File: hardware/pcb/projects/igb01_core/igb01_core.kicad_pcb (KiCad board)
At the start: 2 copper layers, 80 x 80 mm, 108 parts, among them J1 STMP157_GPIO1, J10 I2C_PREV, J11 I2C_NEXT, J12 STMP157_GPIO3, J13 JTAG, J14 USB_CONN, J15 STMP157_GPIO4, J16 Micro_SD_Card, J17 PWR_ON_CON, J18 STMP157_GPIO5, J19 STMP157_GPIO6, J2 BAT_CON, J20 FPA-VZA2-15-LF, J22 Conn_01x13, J3 VBUS_CON, J4 LEFT_CON, J5 RIGHT_CON, J6 STMP157_GPIO2, J7 IGB2_NEXT, J8 IGB3_NEXT, J9 IGB4_NEXT, SW1 SW_DIP_x04, SW2 SW_Push, SW3 SW_Push, U1 W25Q128JVS, U2 AK4619

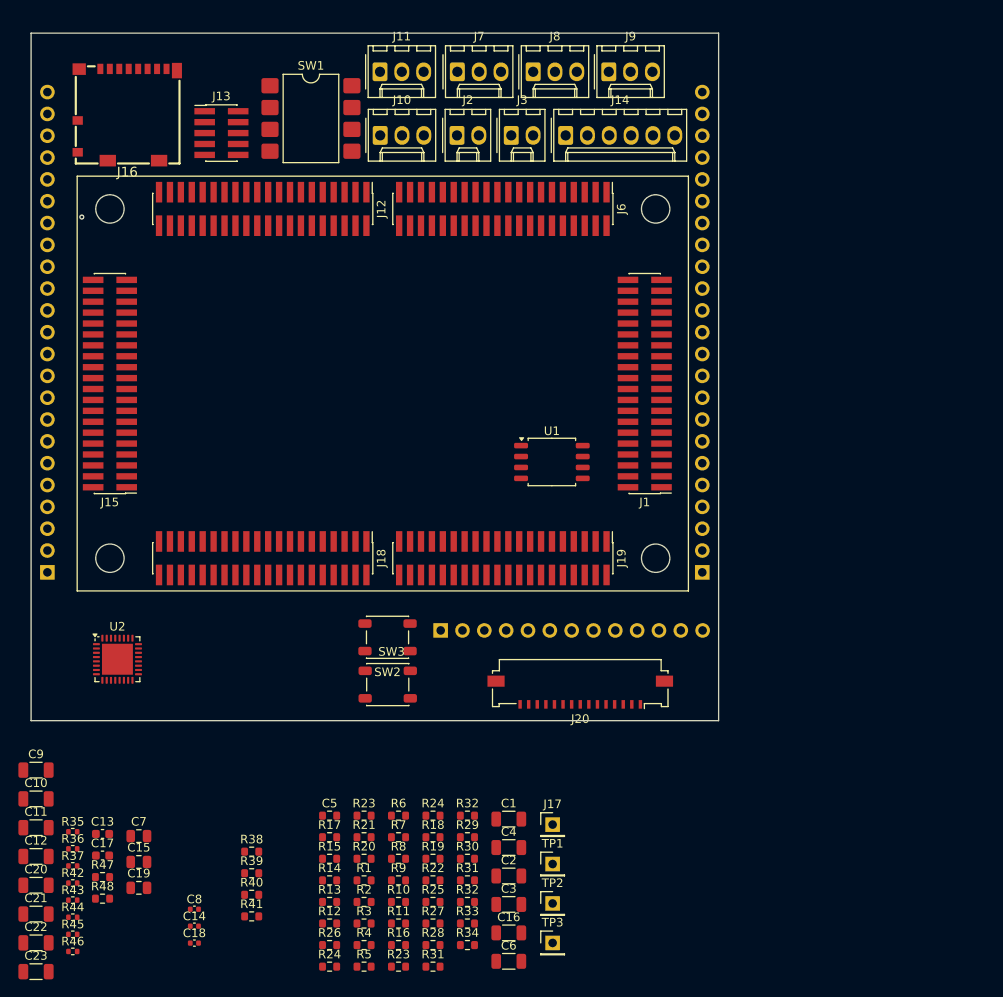
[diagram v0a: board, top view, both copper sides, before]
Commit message: update core board sch&pcb
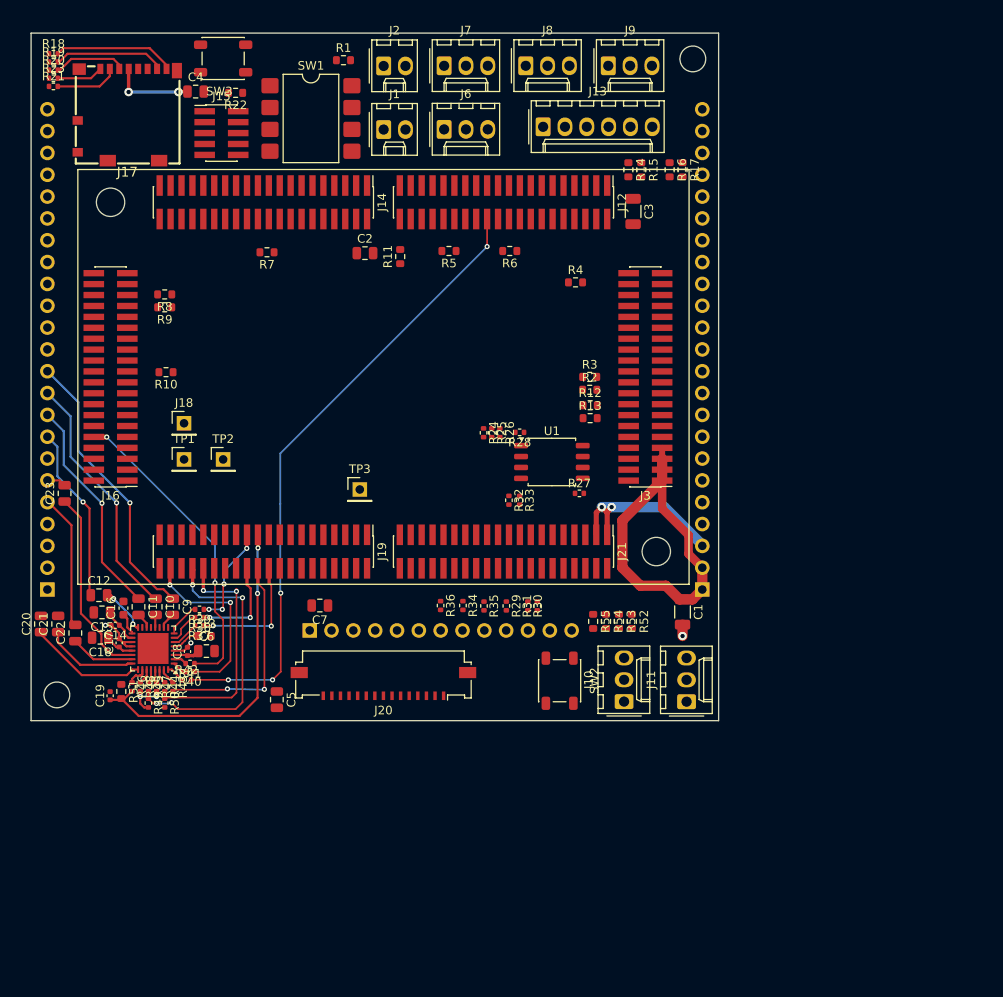
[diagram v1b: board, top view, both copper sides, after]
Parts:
- removed the C16 at (143.9, 165.3)
- removed the C4 at (143.9, 155.4)
- removed the C6 at (143.9, 168.7)
- removed the J17 at (149.0, 152.7)
- removed the R18 at (135.1, 154.2)
- removed the R19 at (135.1, 156.7)
- removed the R22 at (135.1, 159.2)
- removed the R23 at (131.1, 169.3)
- removed the R24 at (135.1, 151.7)
- removed the R25 at (135.1, 161.7)
- removed the R27 at (135.1, 164.2)
- removed the R28 at (135.1, 166.8)
- removed the R31 at (139.1, 159.2)
- removed the R31 at (135.1, 169.3)
- removed the R32 at (139.1, 161.7)
- removed the R32 at (139.1, 151.7)
- removed the REF** at (97.5, 121.7)
- removed the REF** at (161.0, 81.1)
- added C19: 100n, Capacitor_SMD:C_0402_1005Metric, F.Cu at (97.5, 137.8)
- added C5: 47u, Capacitor_SMD:C_0805_2012Metric, F.Cu at (117.0, 138.2)
- added C7: 47u, Capacitor_SMD:C_0805_2012Metric, F.Cu at (122.0, 127.2)
- added J18: PWR_ON_CON, Connector_PinHeader_2.54mm:PinHeader_1x01_P2.54mm_Vertical, F.Cu at (106.2, 106.0)
- added J6: IGB2_PREV, Connector_Molex:Molex_KK-254_AE-6410-03A_1x03_P2.54mm_Vertical, F.Cu at (136.4, 71.8)
- added R14: 22, Resistor_SMD:R_0603_1608Metric, F.Cu at (157.8, 76.5)
- added R15: 22, Resistor_SMD:R_0603_1608Metric, F.Cu at (159.3, 76.5)
- added R16: 22, Resistor_SMD:R_0603_1608Metric, F.Cu at (162.7, 76.5)
- added R17: 22, Resistor_SMD:R_0603_1608Metric, F.Cu at (164.2, 76.5)
- added R2: 22, Resistor_SMD:R_0603_1608Metric, F.Cu at (153.3, 102.2)
- added R3: 22, Resistor_SMD:R_0603_1608Metric, F.Cu at (153.3, 100.7)
- added R31: 10k, Resistor_SMD:R_0402_1005Metric, F.Cu at (147.2, 127.3)
- added R32: 10k, Resistor_SMD:R_0402_1005Metric, F.Cu at (143.9, 115.0)
- added R35: 10k, Resistor_SMD:R_0402_1005Metric, F.Cu at (141.1, 127.3)
- added R36: 10k, Resistor_SMD:R_0402_1005Metric, F.Cu at (136.0, 127.2)
- added R41: 22, Resistor_SMD:R_0402_1005Metric, F.Cu at (106.8, 134.0)
- added R42: 22, Resistor_SMD:R_0402_1005Metric, F.Cu at (106.5, 135.9)
- added R47: 10k, Resistor_SMD:R_0402_1005Metric, F.Cu at (103.0, 136.7)
- added R48: 10k, Resistor_SMD:R_0402_1005Metric, F.Cu at (101.0, 136.7)
- added R51: 10k, Resistor_SMD:R_0603_1608Metric, F.Cu at (98.8, 137.2)
- added REF**: NPTH-3mm, kicadlib:NPTH-3mm, F.Cu at (91.3, 137.7)
- added REF**: NPTH-3mm, kicadlib:NPTH-3mm, F.Cu at (165.3, 63.6)
- C1: footprint Resistor_SMD:R_1206_3216Metric -> Capacitor_SMD:C_1206_3216Metric
- C10, C11, C12, C20, C21, C22, C23, C9: footprint Capacitor_SMD:C_1206_3216Metric -> Capacitor_SMD:C_0805_2012Metric
- C2: footprint Resistor_SMD:R_1206_3216Metric -> Capacitor_SMD:C_0805_2012Metric
- C3: value 47u -> 100u; footprint Resistor_SMD:R_1206_3216Metric -> Capacitor_SMD:C_1206_3216Metric
- C4: renamed from C5; value 100n -> 47u; footprint Resistor_SMD:R_0603_1608Metric -> Capacitor_SMD:C_0805_2012Metric
- R18: renamed from R12; value 10k -> 47k; footprint Resistor_SMD:R_0603_1608Metric -> Resistor_SMD:R_0402_1005Metric
- R19: renamed from R13; value 10k -> 47k; footprint Resistor_SMD:R_0603_1608Metric -> Resistor_SMD:R_0402_1005Metric
- R20: renamed from R14; value 10k -> 47k; footprint Resistor_SMD:R_0603_1608Metric -> Resistor_SMD:R_0402_1005Metric
- R21: renamed from R15; value 10k -> 47k; footprint Resistor_SMD:R_0603_1608Metric -> Resistor_SMD:R_0402_1005Metric
- R23: renamed from R17; value 10k -> 47k; footprint Resistor_SMD:R_0603_1608Metric -> Resistor_SMD:R_0402_1005Metric
- R24: renamed from R20; value 10k -> 47k; footprint Resistor_SMD:R_0603_1608Metric -> Resistor_SMD:R_0402_1005Metric
- R25: renamed from R21; value 10k -> 47k; footprint Resistor_SMD:R_0603_1608Metric -> Resistor_SMD:R_0402_1005Metric
- R26: renamed from R23; value 10k -> 47k; footprint Resistor_SMD:R_0603_1608Metric -> Resistor_SMD:R_0402_1005Metric
- R27: renamed from R24; value 10k -> 47k; footprint Resistor_SMD:R_0603_1608Metric -> Resistor_SMD:R_0402_1005Metric
- R28: renamed from R26; value 10k -> 47k; footprint Resistor_SMD:R_0603_1608Metric -> Resistor_SMD:R_0402_1005Metric
- R29, R30, R33, R34: footprint Resistor_SMD:R_0603_1608Metric -> Resistor_SMD:R_0402_1005Metric
- R4: renamed from R2; value 47 -> 22
- R49: renamed from R47; footprint Resistor_SMD:R_0603_1608Metric -> Resistor_SMD:R_0402_1005Metric
- R5: renamed from R3; value 47 -> 22
- R50: renamed from R48; footprint Resistor_SMD:R_0603_1608Metric -> Resistor_SMD:R_0402_1005Metric
- R6: renamed from R4; value 47 -> 22
- R7: renamed from R5; value 47 -> 22
- R8: renamed from R6; value 47 -> 22
- R9: renamed from R7; value 47 -> 22
- moved R18 106.2 mm to (91.0, 63.0)
- moved R19 102.9 mm to (91.0, 64.0)
- moved R22 101.0 mm to (112.2, 67.6), turned to 180 degrees
- moved R20 99.6 mm to (91.0, 65.0)
- moved R1 95.5 mm to (124.7, 63.8)
- moved R21 95.4 mm to (91.0, 66.8)
- moved R23 94.0 mm to (91.0, 65.9)
- moved C4 85.7 mm to (107.5, 67.5)
- moved R7 83.9 mm to (115.8, 86.2), turned to 180 degrees
- moved R6 82.5 mm to (144.1, 86.0), turned to 180 degrees
- moved C3 81.9 mm to (158.4, 81.4), turned to -90 degrees
- moved J11 81.5 mm to (164.6, 138.4), turned to 90 degrees
- moved R5 78.9 mm to (137.0, 86.0), turned to 180 degrees
- moved R4 76.2 mm to (151.7, 89.7)
- moved SW3 75.3 mm to (110.7, 63.6), turned to 180 degrees
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- renumbered C17 to C16, C18 to C17, C19 to C18, C7 to C6, J2 to J1, J6 to J12, J14 to J13, J12 to J14, J13 to J15, J15 to J16, J16 to J17, J18 to J19, J3 to J2, J19 to J21, J1 to J3, R8 to R10, R9 to R11, R10 to R12, R11 to R13, R16 to R22, R35 to R37, R36 to R38, R37 to R39, R42 to R40, R38 to R52, R39 to R53, R40 to R54, R41 to R55
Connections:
- C17 pad 1: Net-(U2-VREFH) -> +3.3VA
- C18 pad 1: Net-(U2-VREFH) -> +3.3VA
- C3 pad 1: GND -> VBUS
- C3 pad 2: VBUS -> GND
- J10 pad 1: GND -> Net-(J10-Pin_1)
- J10 pad 2: Net-(J10-Pin_2) -> GND
- J11 pad 1: GND -> Net-(J11-Pin_1)
- J11 pad 2: Net-(J11-Pin_2) -> GND
- J12 pad 24: unconnected-(J6-Pin_24-Pad24) -> /SAI1_SD_A
- J13 pad 1: /USB1_D+ -> Net-(J13-Pin_1)
- J13 pad 2: /USB1_D- -> Net-(J13-Pin_2)
- J13 pad 5: /USB_OTG_FS_D+ -> Net-(J13-Pin_5)
- J13 pad 6: /USB_OTG_FS_D- -> Net-(J13-Pin_6)
- J16 pad 10: unconnected-(J15-Pin_10-Pad10) -> / SAI1_SD_B
- J21 pad 11: /EXT_GPIO2 -> unconnected-(J21-Pin_11-Pad11)
- J21 pad 13: /EXT_GPIO3 -> unconnected-(J21-Pin_13-Pad13)
- J21 pad 14: /EXT_GPIO5 -> unconnected-(J21-Pin_14-Pad14)
- J21 pad 15: /EXT_GPIO4 -> unconnected-(J21-Pin_15-Pad15)
- J21 pad 22: /EXT_GPIO6 -> unconnected-(J21-Pin_22-Pad22)
- J21 pad 24: /EXT_GPIO7 -> unconnected-(J21-Pin_24-Pad24)
- J21 pad 7: /EXT_GPIO0 -> unconnected-(J21-Pin_7-Pad7)
- J21 pad 9: /EXT_GPIO1 -> unconnected-(J21-Pin_9-Pad9)
- J4 pad 6: /USART4_RX -> GND
- J4 pad 7: /USART4_TX -> GND
- J5 pad 10: /OUT2L -> /IN2L
- J5 pad 11: /OUT2R -> /IN2R
- J5 pad 3: /IN1L -> /OUT2R
- J5 pad 4: /IN1R -> /OUT2L
- J5 pad 5: /IN2L -> /OUT1R
- J5 pad 6: /IN2R -> /OUT1L
- J5 pad 8: /OUT1L -> /IN1L
- J5 pad 9: /OUT1R -> /IN1R
- J7 pad 1: GND -> Net-(J7-Pin_1)
- J7 pad 2: Net-(J7-Pin_2) -> GND
- J8 pad 1: GND -> Net-(J8-Pin_1)
- J8 pad 2: Net-(J8-Pin_2) -> GND
- J9 pad 1: GND -> Net-(J9-Pin_1)
- J9 pad 2: Net-(J9-Pin_2) -> GND
- R10 pad 1: Net-(J10-Pin_2) -> Net-(J10-Pin_1)
- R12 pad 1: Net-(J11-Pin_2) -> Net-(J11-Pin_1)
- R29 pad 2: /SPI5_MOSI -> /I2C6_SDA
- R30 pad 2: /SPI5_NSS -> /I2C6_SCL
- R33 pad 2: /LCD_BL -> /SPI5_MISO
- R34 pad 2: /LCD_DC -> /LCD_RST
- R4 pad 1: Net-(J7-Pin_2) -> Net-(J7-Pin_1)
- R6 pad 1: Net-(J8-Pin_2) -> Net-(J8-Pin_1)
- R8 pad 1: Net-(J9-Pin_2) -> Net-(J9-Pin_1)
- U2 pad 2: GND -> Net-(U2-SDIN2)
- U2 pad 21: Net-(U2-VREFH) -> +3.3VA
- U2 pad 27: GND -> Net-(U2-I2CAD/CS)
- U2 pad 29: unconnected-(U2-MOSI-Pad29) -> Net-(U2-MOSI)
- U2 pad 32: unconnected-(U2-SDOUT2-Pad32) -> Net-(U2-SDOUT2)
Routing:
- net /SAI1_SD_A: track 0.00 -> 73.6 mm, vias 0 -> 4
- net +5V: track 0.00 -> 43.0 mm
- net /CODEC_PDN: track 0.00 -> 39.5 mm, vias 0 -> 2
- net +3.3V: track 0.00 -> 39.2 mm, vias 0 -> 6
- net / SAI1_SD_B: track 0.00 -> 36.4 mm, vias 0 -> 2
- net /I2C2_SCL: track 0.00 -> 33.8 mm, vias 0 -> 4
- net /IN2R: track 0.00 -> 32.9 mm, vias 0 -> 1
- net /IN2L: track 0.00 -> 29.2 mm, vias 0 -> 1
- net /I2C2_SDA: track 0.00 -> 28.4 mm, vias 0 -> 2
- net /IN1R: track 0.00 -> 25.8 mm, vias 0 -> 1
- net /SAI2_SD_A: track 0.00 -> 25.3 mm, vias 0 -> 2
- net Net-(U2-AOUT1L): track 0.00 -> 22.4 mm
- net /SAI2_SD_B: track 0.00 -> 21.4 mm, vias 0 -> 2
- net /IN1L: track 0.00 -> 20.5 mm, vias 0 -> 1
- net /OUT1R: track 0.00 -> 15.7 mm
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
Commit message: add CAN connector to core board
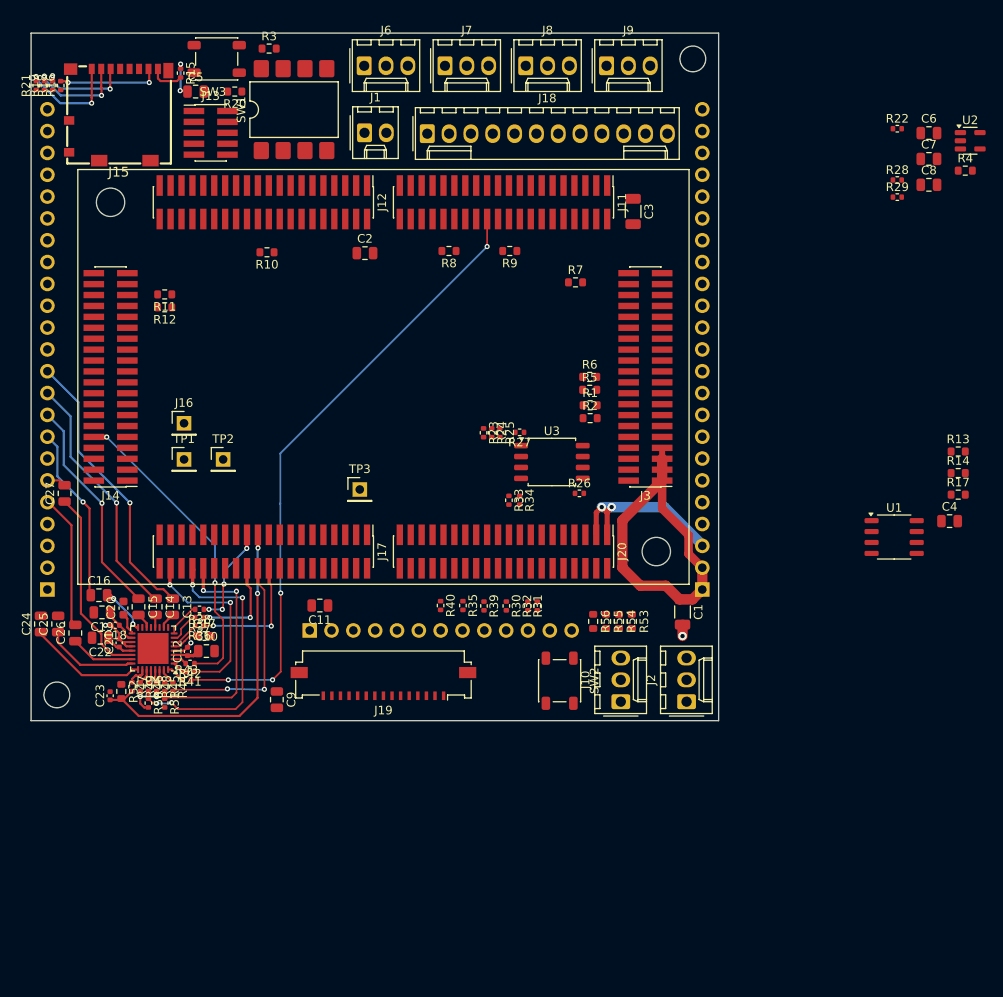
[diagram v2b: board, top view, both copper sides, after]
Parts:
- removed the J2 at (129.4, 64.5)
- removed the R10 at (104.0, 100.1)
- removed the R11 at (131.3, 86.7)
- removed the R15 at (159.3, 76.5)
- removed the R16 at (162.7, 76.5)
- added C4: 100n, Capacitor_SMD:C_0805_2012Metric, F.Cu at (195.2, 117.4)
- added C6: 100n, Capacitor_SMD:C_0805_2012Metric, F.Cu at (192.8, 72.3)
- added C7: 47u, Capacitor_SMD:C_0805_2012Metric, F.Cu at (192.8, 75.3)
- added C8: 47u, Capacitor_SMD:C_0805_2012Metric, F.Cu at (192.8, 78.3)
- added R13: 680, Resistor_SMD:R_0603_1608Metric, F.Cu at (196.2, 109.3)
- added R22: 47k, Resistor_SMD:R_0402_1005Metric, F.Cu at (189.1, 71.8)
- added R28: 10k, Resistor_SMD:R_0402_1005Metric, F.Cu at (189.1, 77.7)
- added R29: 10k, Resistor_SMD:R_0402_1005Metric, F.Cu at (189.1, 79.7)
- added R4: 0, Resistor_SMD:R_0603_1608Metric, F.Cu at (197.1, 76.7)
- added U1: SIT1050T, Package_SO:SOP-8_3.9x4.9mm_P1.27mm, F.Cu at (188.8, 119.3)
- added U2: TPS2041B, Package_TO_SOT_SMD:SOT-23-5, F.Cu at (197.6, 73.2)
- J10: value I2C_PREV -> CAN
- J18: renamed from J13; footprint Connector_Molex:Molex_KK-254_AE-6410-06A_1x06_P2.54mm_Vertical -> Connector_Molex:Molex_KK-254_AE-6410-12A_1x12_P2.54mm_Vertical
- J2: renamed from J11; value I2C_NEXT -> I2C
- J6: value IGB2_PREV -> IGB_PREV
- J7: value IGB2_NEXT -> IGB_NEXT
- J8: value IGB3_NEXT -> IGB2_NEXT
- J9: value IGB4_NEXT -> IGB3_NEXT
- R1: renamed from R12; value 47 -> 22
- R14: value 22 -> 330
- R17: value 22 -> 680
- R2: renamed from R13; value 47 -> 22
- R32: renamed from R31; value 10k -> 47k
- R33: renamed from R32; value 10k -> 47k
- R34: renamed from R33; value 10k -> 47k
- R35: renamed from R34; value 10k -> 47k
- R39: renamed from R35; value 10k -> 47k
- R40: renamed from R36; value 10k -> 47k
- moved R14 52.1 mm to (196.2, 111.8), turned to 0 degrees
- moved R17 49.6 mm to (196.2, 114.3), turned to 0 degrees
- moved R15 15.0 mm to (105.8, 65.3), turned to -90 degrees
- moved J18 13.5 mm to (134.4, 72.3)
- moved J6 11.9 mm to (127.1, 64.5)
- moved R3 8.75 mm to (116.0, 62.5)
- moved R16 2.88 mm to (91.8, 66.8), turned to 90 degrees
- moved J1 2.26 mm to (127.2, 72.2)
- moved SW1 2.22 mm to (119.0, 69.5), turned to 90 degrees
- moved R21 2.17 mm to (89.0, 66.8), turned to 90 degrees
- moved R18 1.80 mm to (90.8, 66.8), turned to 90 degrees
- moved J13 1.25 mm to (109.2, 72.2)
- moved R19 1.05 mm to (89.9, 66.8), turned to 90 degrees
- moved J15 1.00 mm to (98.5, 70.2)
- moved SW3 0.75 mm to (110.0, 63.6)
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- renumbered C6 to C10, C7 to C11, C8 to C12, C9 to C13, C10 to C14, C11 to C15, C12 to C16, C13 to C17, C14 to C18, C15 to C19, C16 to C20, C17 to C21, C18 to C22, C19 to C23, C20 to C24, C21 to C25, C22 to C26, C23 to C27, C4 to C5, C5 to C9, J12 to J11, J14 to J12, J15 to J13, J16 to J14, J17 to J15, J18 to J16, J19 to J17, J20 to J19, J21 to J20, J22 to J21, R7 to R10, R8 to R11, R9 to R12, R18 to R15, R19 to R16, R20 to R18, R21 to R19, R22 to R20, R23 to R21, R24 to R23, R25 to R24, R26 to R25, R27 to R26, R28 to R27, R1 to R3, R29 to R30, R30 to R31, R37 to R36, R38 to R37, R39 to R38, R40 to R41, R41 to R42, R42 to R43, R43 to R44, R44 to R45, R45 to R46, R46 to R47, R47 to R48, R48 to R49, R2 to R5, R49 to R50, R50 to R51, R51 to R52, R52 to R53, R53 to R54, R54 to R55, R55 to R56, R3 to R6, R4 to R7, R5 to R8, R6 to R9, U1 to U3, U2 to U4
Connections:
- J10 pad 2: GND -> Net-(J10-Pin_2)
- J10 pad 3: Net-(J10-Pin_3) -> GND
- J11 pad 15: unconnected-(J12-Pin_15-Pad15) -> /USB_OTG_FS_ID
- J11 pad 17: unconnected-(J12-Pin_17-Pad17) -> /USB1_OC_DETECT
- J11 pad 23: unconnected-(J12-Pin_23-Pad23) -> /USB1_DRV
- J11 pad 25: unconnected-(J12-Pin_25-Pad25) -> /USB2_D-
- J11 pad 27: unconnected-(J12-Pin_27-Pad27) -> /USB2_D+
- J11 pad 40: /I2C3_SDA -> unconnected-(J11-Pin_40-Pad40)
- J11 pad 9: unconnected-(J12-Pin_9-Pad9) -> Net-(J11-Pin_9)
- J14 pad 22: /I2C3_SCL -> unconnected-(J14-Pin_22-Pad22)
- J18 pad 1: Net-(J13-Pin_1) -> /USB1_D+
- J18 pad 2: Net-(J13-Pin_2) -> /USB1_D-
- J18 pad 3: +5V -> Net-(J18-Pin_3)
- J18 pad 5: Net-(J13-Pin_5) -> /USB2_D+
- J18 pad 6: Net-(J13-Pin_6) -> /USB2_D-
- J3 pad 29: unconnected-(J3-Pin_29-Pad29) -> /CAN1_TX
- J3 pad 31: unconnected-(J3-Pin_31-Pad31) -> /CAN1_RX
- J3 pad 33: unconnected-(J3-Pin_33-Pad33) -> /CAN1_STBY
- J4 pad 3: +3.3V -> +5V
- J4 pad 4: GND -> +3.3V
- R14 pad 1: Net-(J13-Pin_1) -> Net-(U1-RxD)
- R14 pad 2: /USB1_D+ -> /CAN1_RX
- R17 pad 1: Net-(J13-Pin_6) -> GND
- R17 pad 2: /USB_OTG_FS_D- -> /CAN1_RX
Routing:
- net /SDMMC1_D1: track 14.2 -> 4.04 mm
- net /SDMMC1_D2: track 5.40 -> 12.4 mm, vias 0 -> 2
- net +3.3V: track 39.2 -> 34.2 mm
- net /SDMMC1_D3: track 7.39 -> 11.5 mm, vias 0 -> 2
- net /SDMMC1_CMD: track 8.46 -> 10.7 mm, vias 0 -> 2
- net /SDMMC1_D0: track 13.0 -> 12.0 mm, vias 0 -> 2

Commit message: change header pin assignment for core board
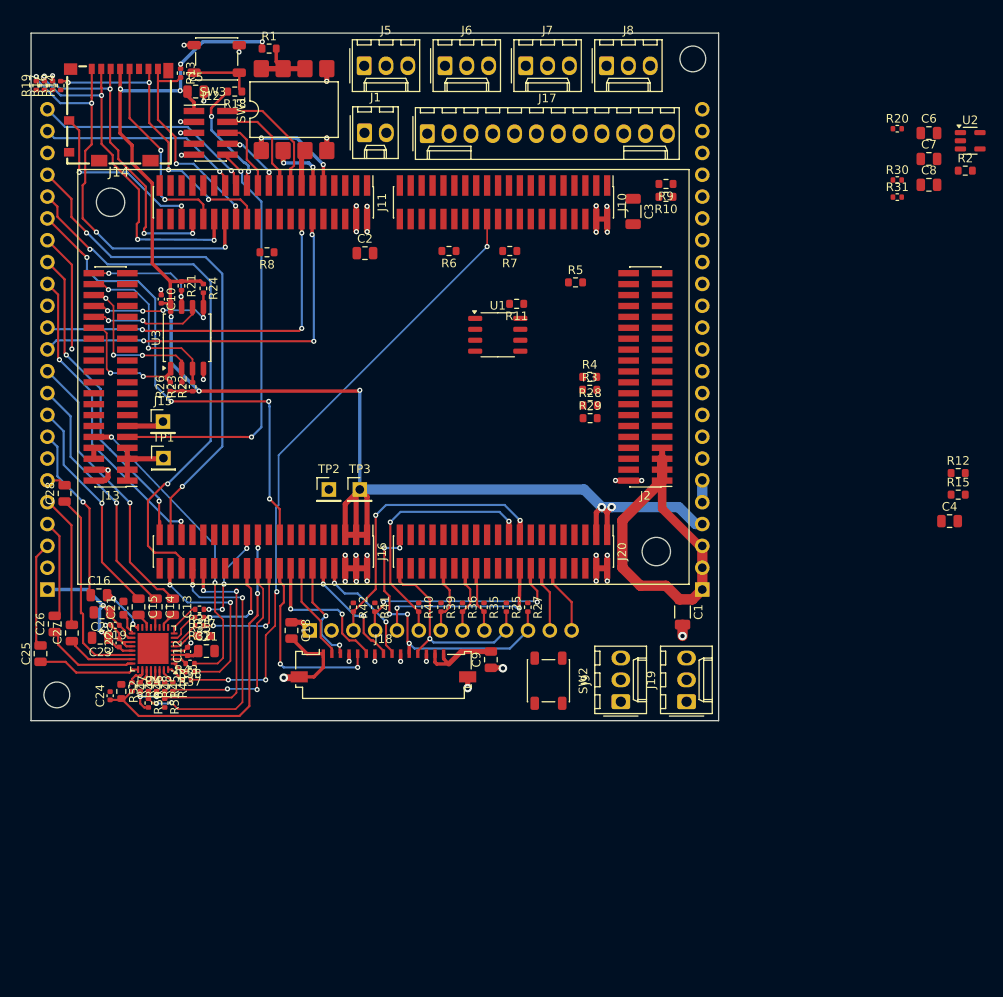
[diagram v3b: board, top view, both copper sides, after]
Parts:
- removed R53, R54, R55, R56: 0, Resistor_SMD:R_0603_1608Metric
- added C10: 100n, Capacitor_SMD:C_0402_1005Metric, F.Cu at (103.5, 91.6)
- moved R10 59.7 mm to (162.2, 79.7)
- moved R9 59.7 mm to (162.2, 78.2)
- moved R11 54.2 mm to (144.8, 92.2), turned to 180 degrees
- moved U1 51.8 mm to (142.7, 95.8)
- moved R24 49.8 mm to (108.4, 90.3), turned to -90 degrees
- moved U3 44.8 mm to (106.5, 96.1), turned to 90 degrees
- moved R26 41.0 mm to (104.5, 101.8), turned to 90 degrees
- moved R21 39.1 mm to (105.8, 90.0)
- moved R23 37.4 mm to (105.9, 101.8), turned to 90 degrees
- moved R22 35.2 mm to (107.2, 101.8), turned to 90 degrees
- moved C9 25.3 mm to (141.8, 133.6), turned to 90 degrees
- moved R42 23.0 mm to (125.8, 127.5)
- moved R41 18.9 mm to (128.3, 127.5), turned to -90 degrees
- moved R40 16.3 mm to (133.4, 127.5)
- moved TP2 12.8 mm to (123.0, 113.8)
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- renumbered C10 to C11, C11 to C18, C18 to C19, C19 to C20, C20 to C21, C21 to C22, C22 to C23, C23 to C24, C24 to C25, C25 to C26, C26 to C27, C27 to C28, J11 to J10, J12 to J11, J13 to J12, J14 to J13, J15 to J14, J16 to J15, J17 to J16, J18 to J17, J19 to J18, J2 to J19, J3 to J2, J4 to J3, J5 to J4, J6 to J5, J7 to J6, J8 to J7, J9 to J8, J10 to J9, R3 to R1, R12 to R10, R13 to R11, R14 to R12, R15 to R13, R16 to R14, R17 to R15, R18 to R16, R19 to R17, R20 to R18, R21 to R19, R4 to R2, R22 to R20, R23 to R21, R24 to R22, R25 to R23, R26 to R24, R30 to R25, R27 to R26, R31 to R27, R1 to R28, R2 to R29, R5 to R3, R28 to R30, R29 to R31, R36 to R32, R37 to R33, R38 to R34, R39 to R35, R35 to R36, R41 to R37, R42 to R38, R40 to R39, R6 to R4, R33 to R40, R32 to R41, R34 to R42, R7 to R5, R8 to R6, R9 to R7, R10 to R8, R11 to R9
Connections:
- J18 pad 11: /I2C6_SCL -> /I2C1_SCL
- J18 pad 12: /I2C6_SDA -> /I2C1_SDA
- J20 pad 10: /CONF_BIT2 -> unconnected-(J20-Pin_10-Pad10)
- J20 pad 12: /CONF_BIT3 -> /LCD_TP_RST
- J20 pad 14: unconnected-(J20-Pin_14-Pad14) -> /LCD_TP_INT
- J20 pad 20: /LCD_DC -> unconnected-(J20-Pin_20-Pad20)
- J20 pad 21: /LCD_BL -> unconnected-(J20-Pin_21-Pad21)
- J20 pad 23: /LCD_RST -> unconnected-(J20-Pin_23-Pad23)
- J20 pad 25: /LCD_TP_INT -> unconnected-(J20-Pin_25-Pad25)
- J20 pad 26: unconnected-(J20-Pin_26-Pad26) -> /LCD_BL
- J20 pad 27: /LCD_TP_RST -> unconnected-(J20-Pin_27-Pad27)
- J20 pad 28: unconnected-(J20-Pin_28-Pad28) -> /LCD_RST
- J20 pad 32: unconnected-(J20-Pin_32-Pad32) -> /LCD_DC
- J20 pad 6: /CONF_BIT0 -> unconnected-(J20-Pin_6-Pad6)
- J20 pad 8: /CONF_BIT1 -> unconnected-(J20-Pin_8-Pad8)
- J21 pad 10: /I2C6_SDA -> /I2C1_SDA
- J21 pad 11: /I2C6_SCL -> /I2C1_SCL
- J3 pad 10: /USART3_RX -> /USART3_TX
- J3 pad 11: /USART3_TX -> GND
- J3 pad 12: GND -> /SPI4_GPIO_CS1
- J3 pad 13: /SDMMC3_D0 -> /SPI4_NSS
- J3 pad 14: /SDMMC3_D1 -> /SPI4_MOSI
- J3 pad 15: /SDMMC3_D2 -> /SPI4_MISO
- J3 pad 16: /SDMMC3_D3 -> /SPI4_SCK
- J3 pad 17: /SDMMC3_CK -> GND
- J3 pad 18: /SDMMC3_CMD -> /SPI2_NSS
- J3 pad 19: /SPI2_NSS -> /SPI2_MOSI
- J3 pad 20: /SPI2_MOSI -> /SPI2_MISO
- J3 pad 21: /SPI2_MISO -> /SPI2_SCK
- J3 pad 22: /SPI2_SCK -> /GPIO_CLOCK_OUT
- J3 pad 23: GND -> /GPIO_RESET_OUT
- J3 pad 7: GND -> /USART1_RX
- J3 pad 8: /USART1_RX -> /USART1_TX
- J3 pad 9: /USART1_TX -> /USART3_RX
- J4 pad 15: /I2C1_SDA -> /SDMMC3_D0
- J4 pad 16: /I2C1_SCL -> /SDMMC3_D1
- J4 pad 17: /SPI4_GPIO_CS1 -> /SDMMC3_D2
- J4 pad 18: /SPI4_NSS -> /SDMMC3_D3
- J4 pad 19: /SPI4_MOSI -> /SDMMC3_CK
- J4 pad 20: /SPI4_MISO -> /SDMMC3_CMD
- J4 pad 21: /SPI4_SCK -> GND
- J4 pad 22: /GPIO_CLOCK_OUT -> /I2C6_SCL
- J4 pad 23: /GPIO_RESET_OUT -> /I2C6_SDA
- R25 pad 2: /I2C6_SDA -> /I2C1_SDA
- R27 pad 2: /I2C6_SCL -> /I2C1_SCL
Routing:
- net +3.3V: track 34.2 -> 195.0 mm, vias 6 -> 11
- net GND: track 3.87 -> 76.0 mm, vias 2 -> 40
- net /SDMMC3_CK: track 0.00 -> 63.4 mm, vias 0 -> 2
- net /SDMMC3_CMD: track 0.00 -> 59.3 mm, vias 0 -> 2
- net /SDMMC3_D3: track 0.00 -> 57.4 mm, vias 0 -> 4
- net /NRST: track 0.00 -> 57.0 mm, vias 0 -> 2
- net /ADC1_INP1: track 0.00 -> 45.8 mm, vias 0 -> 3
- net /ADC2_INP18: track 0.00 -> 42.6 mm, vias 0 -> 3
- net /SDMMC3_D1: track 0.00 -> 37.2 mm, vias 0 -> 2
- net /SDMMC3_D0: track 0.00 -> 36.5 mm, vias 0 -> 2
- net /SDMMC1_D2: track 12.4 -> 47.7 mm, vias 2 -> 4
- net /I2C1_SCL: track 0.00 -> 35.2 mm, vias 0 -> 5
- net /SPI5_MISO: track 0.00 -> 34.2 mm, vias 0 -> 2
- net /SPI5_NSS: track 0.00 -> 30.3 mm, vias 0 -> 2
- net /SDMMC1_D3: track 11.5 -> 41.6 mm, vias 2 -> 4
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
